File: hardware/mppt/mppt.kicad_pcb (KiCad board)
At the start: 4 copper layers, 90 x 50 mm, 116 parts, among them J1401 Conn_01x04, J1402 Conn_01x02, J1403 Conn_02x04_Odd_Even, J1404 Conn_01x11, J1405 USB_C_Plug_USB2.0, J401 Conn_01x04, J402 Conn_01x03, SW201 SW_SPST, U1401 ISO1044BD, U1402 USBLC6-2SC6, U201 STM32F446RETx, U401 MCP9700Ax-ELT, U402 MCP9700Ax-ELT, Y201 16MHz, Y202 32kHz

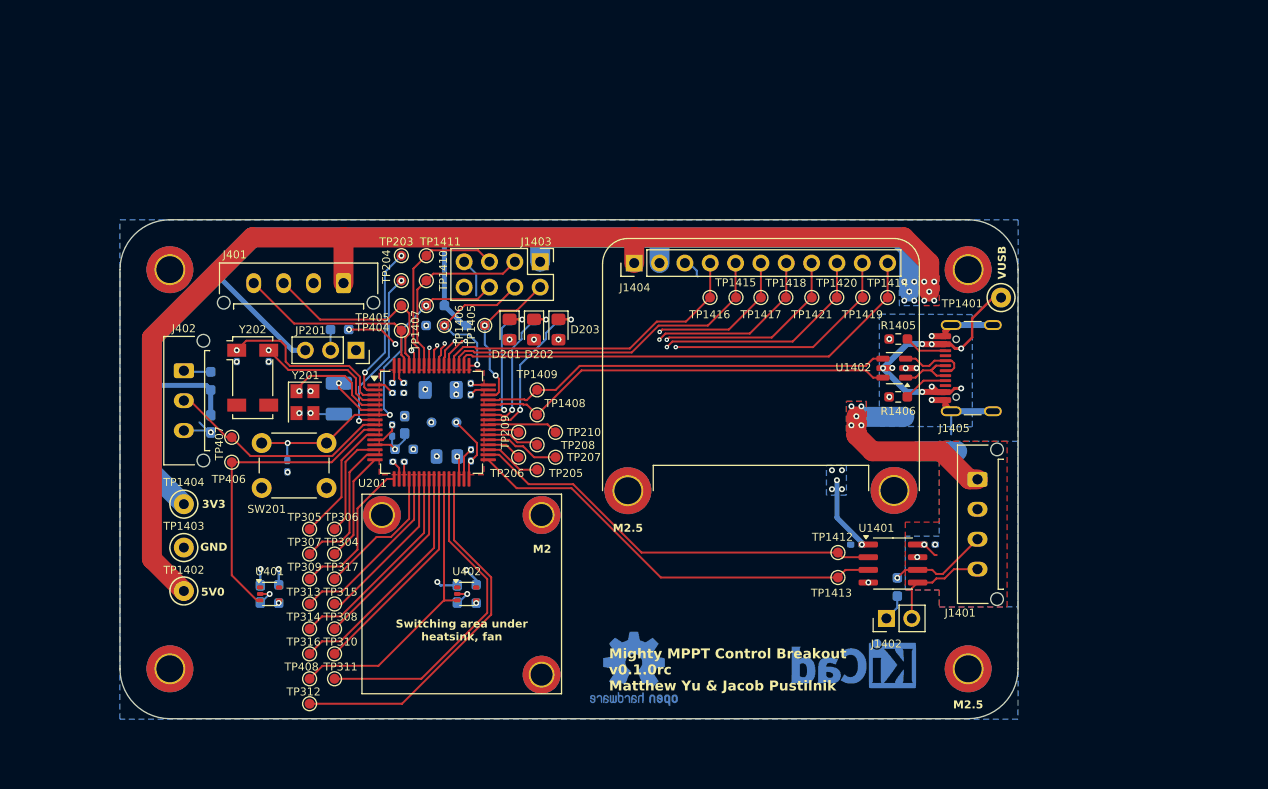
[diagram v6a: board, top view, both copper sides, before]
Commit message: converter schematic and layout.
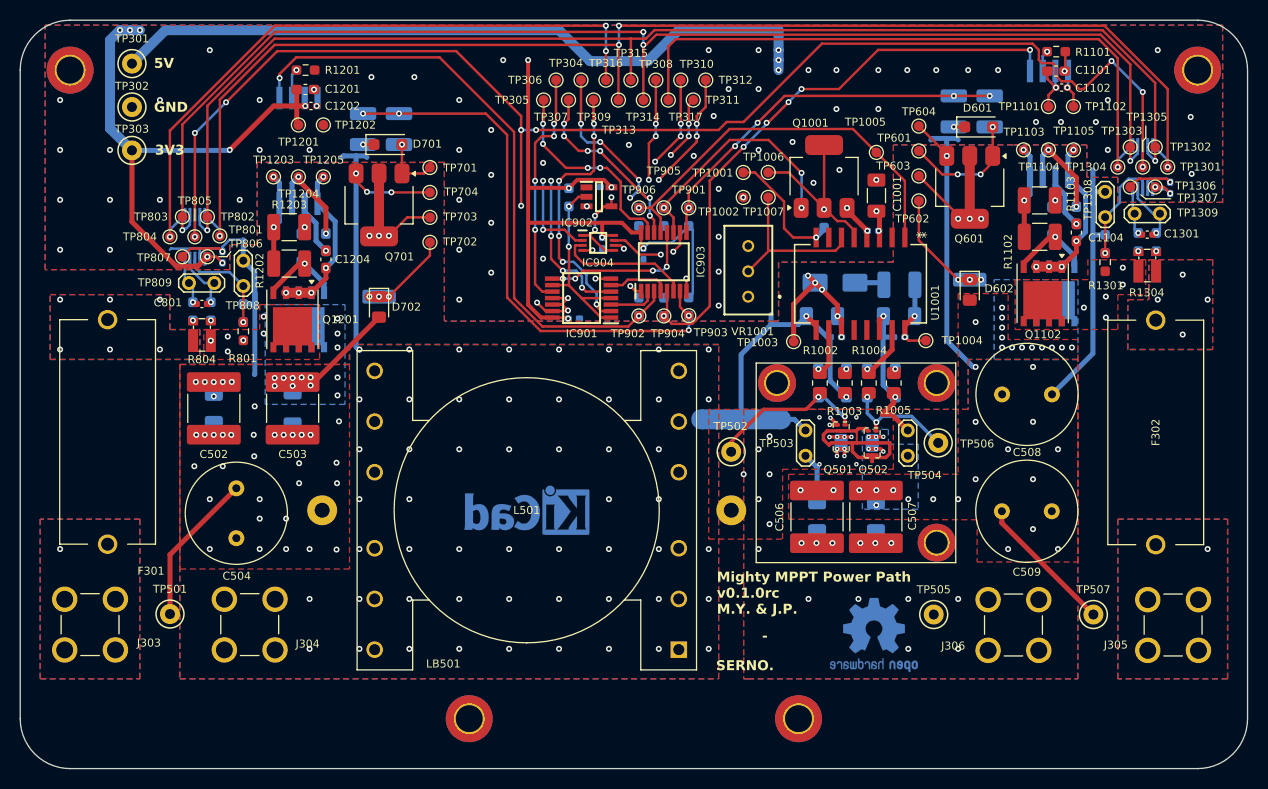
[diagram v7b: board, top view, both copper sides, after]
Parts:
- removed C1401, C1402, C203, C205, C208, C209, C211, C212, C213: 100n, Capacitor_SMD:C_0402_1005Metric_Pad0.74x0.62mm_HandSolder
- removed C201, C206: 10p, Capacitor_SMD:C_0402_1005Metric_Pad0.74x0.62mm_HandSolder
- removed C202, C207: 15p, Capacitor_SMD:C_0402_1005Metric_Pad0.74x0.62mm_HandSolder
- removed C204: 10u, Capacitor_SMD:C_1206_3216Metric_Pad1.33x1.80mm_HandSolder
- removed C210: 4.7u, Capacitor_SMD:C_0805_2012Metric_Pad1.18x1.45mm_HandSolder
- removed C214, C401, C402, C403: 1u, Capacitor_SMD:C_0603_1608Metric_Pad1.08x0.95mm_HandSolder
- removed D201, D202, D203: RED, LED_SMD:LED_0805_2012Metric_Pad1.15x1.40mm_HandSolder
- removed FB201: FerriteBead, Resistor_SMD:R_0603_1608Metric_Pad0.98x0.95mm_HandSolder
- removed H1401, H1402: MountingHole, MountingHole:MountingHole_2.7mm_M2.5_DIN965_Pad_TopBottom
- removed J1401, J401: Conn_01x04, Connector_Molex:Molex_Micro-Fit_3.0_43650-0415_1x04_P3.00mm_Vertical
- removed J1402: Conn_01x02, Connector_PinHeader_2.54mm:PinHeader_1x02_P2.54mm_Vertical
- removed J1403: Conn_02x04_Odd_Even, Connector_PinHeader_2.54mm:PinHeader_2x04_P2.54mm_Vertical
- removed J1404: Conn_01x11, Connector_PinHeader_2.54mm:PinHeader_1x11_P2.54mm_Vertical
- removed J1405: USB_C_Plug_USB2.0, Connector_USB:USB_C_Receptacle_GCT_USB4105-xx-A_16P_TopMnt_Horizontal
- removed J402: Conn_01x03, Connector_Molex:Molex_Micro-Fit_3.0_43650-0315_1x03_P3.00mm_Vertical
- removed JP201: Jumper_3_Bridged12, Connector_PinSocket_2.54mm:PinSocket_1x03_P2.54mm_Vertical
- removed NT1401, NT1402: NetTie_2, NetTie:NetTie-2_SMD_Pad2.0mm
- removed R1401: 120, Resistor_SMD:R_0603_1608Metric_Pad0.98x0.95mm_HandSolder
- removed R1402, R1403, R1404, R204: 100k, Resistor_SMD:R_0603_1608Metric_Pad0.98x0.95mm_HandSolder
- removed R1405, R1406: 5.1k, Resistor_SMD:R_0603_1608Metric_Pad0.98x0.95mm_HandSolder
- removed R201, R202, R205: 3.3k, Resistor_SMD:R_0603_1608Metric_Pad0.98x0.95mm_HandSolder
- removed R203: 0, Resistor_SMD:R_1210_3225Metric_Pad1.30x2.65mm_HandSolder
- removed R401, R402, R403: 205, Resistor_SMD:R_0603_1608Metric_Pad0.98x0.95mm_HandSolder
- removed SW201: SW_SPST, Button_Switch_THT:SW_PUSH_6mm
- removed TP1401, TP1402, TP1403, TP1404: TestPoint, TestPoint:TestPoint_Keystone_5000-5004_Miniature
- removed TP1405, TP1406, TP1407, TP1408, TP1409, TP1410, TP1411, TP1412, TP1413, TP1414, TP1415, TP1416, TP1417, TP1418, TP1419, TP1420, TP1421, TP201, TP202, TP203, TP204, TP205, TP206, TP207, TP208, TP209, TP210, TP404, TP405, TP406, TP407, TP408: TestPoint_Small, TestPoint:TestPoint_Pad_D1.0mm
- removed U1401: ISO1044BD, Package_SO:SOIC-8_3.9x4.9mm_P1.27mm
- removed U1402: USBLC6-2SC6, Package_TO_SOT_SMD:SOT-23-6
- removed U201: STM32F446RETx, Package_QFP:LQFP-64_10x10mm_P0.5mm
- removed U401, U402: MCP9700Ax-ELT, Package_TO_SOT_SMD:SOT-353_SC-70-5
- removed Y201: 16MHz, Crystal:Crystal_SMD_Abracon_ABM8G-4Pin_3.2x2.5mm
- removed Y202: 32kHz, Crystal:Crystal_SMD_Abracon_ABS25-4Pin_8.0x3.8mm
- added C1001: 10u, Capacitor_SMD:C_1206_3216Metric_Pad1.33x1.80mm_HandSolder, F.Cu at (120.8, 42.6)
- added C1002: 100n, Capacitor_SMD:C_0402_1005Metric_Pad0.74x0.62mm_HandSolder, B.Cu at (120.5, 46.1)
- added C1003: 10u, Capacitor_SMD:C_1206_3216Metric_Pad1.33x1.80mm_HandSolder, B.Cu at (123.1, 54.7)
- added C1004: 10u, Capacitor_SMD:C_1206_3216Metric_Pad1.33x1.80mm_HandSolder, B.Cu at (115.3, 54.7)
- added C1005: 100n, Capacitor_SMD:C_0402_1005Metric_Pad0.74x0.62mm_HandSolder, B.Cu at (123.1, 56.8)
- added C1006: 100n, Capacitor_SMD:C_0402_1005Metric_Pad0.74x0.62mm_HandSolder, B.Cu at (116.7, 56.8)
- added C1101: 1u, Capacitor_SMD:C_0603_1608Metric_Pad1.08x0.95mm_HandSolder, F.Cu at (138.8, 30.1)
- added C1102: 100n, Capacitor_SMD:C_0402_1005Metric_Pad0.74x0.62mm_HandSolder, F.Cu at (139.4, 31.8)
- added C1103: 1u, Capacitor_SMD:C_0603_1608Metric_Pad1.08x0.95mm_HandSolder, B.Cu at (140.8, 44.5)
- added C1104: 1u, Capacitor_SMD:C_0603_1608Metric_Pad1.08x0.95mm_HandSolder, F.Cu at (140.8, 46.3)
- added C1201: 1u, Capacitor_SMD:C_0603_1608Metric_Pad1.08x0.95mm_HandSolder, F.Cu at (63.6, 31.9)
- added C1202: 100n, Capacitor_SMD:C_0402_1005Metric_Pad0.74x0.62mm_HandSolder, F.Cu at (64.1, 33.6)
- added C1203: 1u, Capacitor_SMD:C_0603_1608Metric_Pad1.08x0.95mm_HandSolder, B.Cu at (65.6, 47.2)
- added C1204: 1u, Capacitor_SMD:C_0603_1608Metric_Pad1.08x0.95mm_HandSolder, F.Cu at (65.6, 49.0)
- added C1301: 100n, Capacitor_SMD:C_0402_1005Metric_Pad0.74x0.62mm_HandSolder, F.Cu at (147.9, 46.5)
- added C1302: 100n, Capacitor_SMD:C_0402_1005Metric_Pad0.74x0.62mm_HandSolder, B.Cu at (150.2, 41.8)
- added C501: 100n, Capacitor_SMD:C_1206_3216Metric_Pad1.33x1.80mm_HandSolder, B.Cu at (62.3, 63.9)
- added C502: 1u, Capacitor_SMD:C_2220_5750Metric_Pad1.97x5.40mm_HandSolder, F.Cu at (54.4, 63.9)
- added C503: 2.2u, Capacitor_SMD:C_2220_5750Metric_Pad1.97x5.40mm_HandSolder, F.Cu at (62.3, 63.9)
- added C504: 18u, Capacitor_THT:C_Radial_D10.0mm_H16.0mm_P5.00mm, F.Cu at (56.7, 71.9)
- added C505: 100n, Capacitor_SMD:C_1206_3216Metric_Pad1.33x1.80mm_HandSolder, B.Cu at (118.8, 67.4)
- added C506: 1u, Capacitor_SMD:C_2220_5750Metric_Pad1.97x5.40mm_HandSolder, F.Cu at (114.9, 74.8)
- added C507: 2.2u, Capacitor_SMD:C_2220_5750Metric_Pad1.97x5.40mm_HandSolder, F.Cu at (120.8, 74.8)
- added C508: 18u, Capacitor_THT:C_Radial_D10.0mm_H16.0mm_P5.00mm, F.Cu at (133.4, 62.5)
- added C509: 18u, Capacitor_THT:C_Radial_D10.0mm_H16.0mm_P5.00mm, F.Cu at (133.4, 74.2)
- added C801: 100n, Capacitor_SMD:C_0402_1005Metric_Pad0.74x0.62mm_HandSolder, F.Cu at (53.2, 53.4)
- added C802: 100n, Capacitor_SMD:C_0402_1005Metric_Pad0.74x0.62mm_HandSolder, B.Cu at (55.3, 48.8)
- added C901: 100n, Capacitor_SMD:C_0402_1005Metric_Pad0.74x0.62mm_HandSolder, B.Cu at (90.5, 54.9)
- added C902: 100n, Capacitor_SMD:C_0402_1005Metric_Pad0.74x0.62mm_HandSolder, B.Cu at (93.7, 41.7)
- added C903: 100n, Capacitor_SMD:C_0402_1005Metric_Pad0.74x0.62mm_HandSolder, B.Cu at (97.5, 48.4)
- added C904: 100n, Capacitor_SMD:C_0402_1005Metric_Pad0.74x0.62mm_HandSolder, B.Cu at (93.3, 47.3)
- added D1001: Schottky, Diode_SMD:D_SOD-123F, B.Cu at (116.4, 60.0)
- added D1002: Zener, Diode_SMD:D_SOD-123F, B.Cu at (116.4, 62.8)
- added D1003: Schottky, Diode_SMD:D_SOD-123F, B.Cu at (121.3, 60.0)
- added D1004: 0.62V, Diode_SMD:D_SMA, B.Cu at (116.7, 51.3)
- added D1005: Zener, Diode_SMD:D_SOD-123F, B.Cu at (121.3, 62.8)
- added D1101: Schottky, Diode_SMD:D_SOD-123F, B.Cu at (138.5, 45.1)
- added D1201: Schottky, Diode_SMD:D_SOD-123F, B.Cu at (63.2, 47.8)
- added D501: 150, Diode_SMD:D_SMA, B.Cu at (54.4, 63.9)
- added D502: SMAJ150CA, Diode_SMD:D_SMA, B.Cu at (114.9, 74.8)
- added D503: 150, Diode_SMD:D_SMA, B.Cu at (120.8, 74.8)
- added D601: Schottky, Diode_SMD:D_SOD-123F, F.Cu at (131.1, 35.7)
- added D602: BLU, LED_SMD:LED_0805_2012Metric_Pad1.15x1.40mm_HandSolder, F.Cu at (130.2, 52.0)
- added D701: Schottky, Diode_SMD:D_SOD-123F, F.Cu at (71.9, 37.5)
- added D702: BLU, LED_SMD:LED_0805_2012Metric_Pad1.15x1.40mm_HandSolder, F.Cu at (71.0, 53.7)
- added F301: Fuse, footprints:littelfuse_65600001009, F.Cu at (43.8, 66.3)
- added F302: Fuse, footprints:littelfuse_65600001009, F.Cu at (148.8, 66.3)
- added IC1301: INA229AIDGSR, footprints:ti_INA229_AIDGSR, B.Cu at (147.5, 39.7)
- added IC801: INA229AIDGSR, footprints:ti_INA229_AIDGSR, B.Cu at (52.5, 46.7)
- added IC901: SN74LVC08APWR, footprints:ti_SN74LVC08A_PWR, F.Cu at (91.3, 52.9)
- added IC902: SN74LVC1G04DBVR, footprints:ti_SN74LVC1G04_DBVR, F.Cu at (93.0, 42.7)
- added IC903: SN74HCS367PWR, footprints:ti_SN74HCS367_PWR, F.Cu at (99.5, 49.2)
- added IC904: SN74LVC2G32DCUR, footprints:ti_SN74LVC2G32_DCUR, F.Cu at (92.9, 47.3)
- added J303: CT3151, footprints:caltest_ct3151, F.Cu at (42.0, 85.6)
- added J304: CT3151, footprints:caltest_ct3151, F.Cu at (58.0, 85.6)
- added J305: CT3151, footprints:caltest_ct3151, F.Cu at (150.5, 85.6)
- added J306: CT3151, footprints:caltest_ct3151, F.Cu at (134.5, 85.6)
- added L501: 471u, footprints:ferroxcube_PQ32_20_3C97_wire, F.Cu at (62.8, 74.1)
- added LB501: CPV-PQ32/20-1S-12PD-Z, footprints:ferroxcube_CPV-PQ32_20-1S-12P-Z, F.Cu at (101.0, 88.1)
- added NT1001: NetTie_2, NetTie:NetTie-2_SMD_Pad0.5mm, B.Cu at (110.2, 55.0)
- added NT1301: NetTie_2, NetTie:NetTie-2_SMD_Pad0.5mm, B.Cu at (142.5, 40.5)
- added NT501: NetTie_3_Tee, NetTie:NetTie-3_SMD_Pad2.0mm, B.Cu at (107.2, 65.0)
- added NT601: NetTie_2, NetTie:NetTie-2_SMD_Pad0.5mm, B.Cu at (127.8, 37.4)
- added NT701: NetTie_2, NetTie:NetTie-2_SMD_Pad0.5mm, B.Cu at (68.7, 39.1)
- added NT801: NetTie_2, NetTie:NetTie-2_SMD_Pad0.5mm, B.Cu at (57.4, 47.5)
- added Q1001: Q_NMOS_GDS, Package_TO_SOT_SMD:SOT-223-3_TabPin2, F.Cu at (115.6, 40.7)
- added Q1101: Q_NMOS_SGD, Package_SO:PowerPAK_SO-8_Single, B.Cu at (138.7, 52.4)
- added Q1102: Q_NMOS_SGD, Package_SO:PowerPAK_SO-8_Single, F.Cu at (137.5, 52.4)
- added Q1201: Q_NMOS_SGD, Package_SO:PowerPAK_SO-8_Single, F.Cu at (62.3, 55.0)
- added Q1202: Q_NMOS_SGD, Package_SO:PowerPAK_SO-8_Single, B.Cu at (63.5, 55.0)
- added Q501: EPC2059, footprints:epc_EPC2059, F.Cu at (117.3, 66.8)
- added Q502: EPC2059, footprints:epc_EPC2059, F.Cu at (120.4, 67.4)
- added Q601: Q_NMOS_GDS, Package_TO_SOT_SMD:SOT-223-3_TabPin2, F.Cu at (130.2, 41.7)
- added Q701: Q_NMOS_GDS, Package_TO_SOT_SMD:SOT-223-3_TabPin2, F.Cu at (71.0, 43.5)
- added R1001: 100k, Resistor_SMD:R_0603_1608Metric_Pad0.98x0.95mm_HandSolder, B.Cu at (115.6, 44.9)
- added R1002: 0, Resistor_SMD:R_0805_2012Metric_Pad1.20x1.40mm_HandSolder, F.Cu at (115.1, 61.4)
- added R1003: 0, Resistor_SMD:R_0805_2012Metric_Pad1.20x1.40mm_HandSolder, F.Cu at (117.6, 61.4)
- added R1004: 0, Resistor_SMD:R_0805_2012Metric_Pad1.20x1.40mm_HandSolder, F.Cu at (120.0, 61.4)
- added R1005: 0, Resistor_SMD:R_0805_2012Metric_Pad1.20x1.40mm_HandSolder, F.Cu at (122.5, 61.4)
- added R1006: 1.5, Resistor_SMD:R_1210_3225Metric_Pad1.30x2.65mm_HandSolder, B.Cu at (123.1, 51.5)
- added R1101: 7.32k, Resistor_SMD:R_0603_1608Metric_Pad0.98x0.95mm_HandSolder, F.Cu at (138.8, 28.1)
- added R1102: 15, Resistor_SMD:R_1210_3225Metric_Pad1.30x2.65mm_HandSolder, F.Cu at (137.2, 46.7)
- added R1103: 15, Resistor_SMD:R_1210_3225Metric_Pad1.30x2.65mm_HandSolder, F.Cu at (137.2, 43.1)
- added R1201: 7.32k, Resistor_SMD:R_0603_1608Metric_Pad0.98x0.95mm_HandSolder, F.Cu at (63.6, 30.0)
- added R1202: 15, Resistor_SMD:R_1210_3225Metric_Pad1.30x2.65mm_HandSolder, F.Cu at (62.0, 49.4)
- added R1203: 15, Resistor_SMD:R_1210_3225Metric_Pad1.30x2.65mm_HandSolder, F.Cu at (62.0, 45.7)
- added R1301: 86.6k, Resistor_SMD:R_0603_1608Metric_Pad0.98x0.95mm_HandSolder, F.Cu at (143.7, 49.3)
- added R1302: 100k, Resistor_SMD:R_0603_1608Metric_Pad0.98x0.95mm_HandSolder, B.Cu at (143.7, 47.4)
- added R1303: 15, Resistor_SMD:R_0603_1608Metric_Pad0.98x0.95mm_HandSolder, B.Cu at (147.1, 47.2)
- added R1304: 4m, Resistor_SMD:R_Shunt_Vishay_WSKW0612, F.Cu at (147.9, 49.6)
- added R1305: 15, Resistor_SMD:R_0603_1608Metric_Pad0.98x0.95mm_HandSolder, B.Cu at (148.8, 47.2)
- added R601: 15, Resistor_SMD:R_1210_3225Metric_Pad1.30x2.65mm_HandSolder, B.Cu at (128.6, 34.1)
- added R602: 15, Resistor_SMD:R_1210_3225Metric_Pad1.30x2.65mm_HandSolder, B.Cu at (132.2, 34.1)
- added R603: 10k, Resistor_SMD:R_2512_6332Metric_Pad1.40x3.35mm_HandSolder, B.Cu at (130.2, 48.0)
- added R701: 15, Resistor_SMD:R_1210_3225Metric_Pad1.30x2.65mm_HandSolder, B.Cu at (69.4, 35.9)
- added R702: 15, Resistor_SMD:R_1210_3225Metric_Pad1.30x2.65mm_HandSolder, B.Cu at (73.0, 35.9)
- added R703: 10k, Resistor_SMD:R_2512_6332Metric_Pad1.40x3.35mm_HandSolder, B.Cu at (71.0, 49.7)
- added R801: 86.6k, Resistor_SMD:R_0603_1608Metric_Pad0.98x0.95mm_HandSolder, F.Cu at (57.4, 56.2)
- added R802: 100k, Resistor_SMD:R_0603_1608Metric_Pad0.98x0.95mm_HandSolder, B.Cu at (57.4, 54.4)
- added R803: 15, Resistor_SMD:R_0603_1608Metric_Pad0.98x0.95mm_HandSolder, B.Cu at (52.3, 54.2)
- added R804: 4m, Resistor_SMD:R_Shunt_Vishay_WSKW0612, F.Cu at (53.2, 56.5)
- added R805: 15, Resistor_SMD:R_0603_1608Metric_Pad0.98x0.95mm_HandSolder, B.Cu at (54.1, 54.2)
- added R901: 100k, Resistor_SMD:R_0603_1608Metric_Pad0.98x0.95mm_HandSolder, B.Cu at (90.0, 42.8)
- added R902: 100k, Resistor_SMD:R_0603_1608Metric_Pad0.98x0.95mm_HandSolder, B.Cu at (102.0, 44.7)
- added R903: 100k, Resistor_SMD:R_0603_1608Metric_Pad0.98x0.95mm_HandSolder, B.Cu at (97.0, 53.7)
- added R904: 100k, Resistor_SMD:R_0603_1608Metric_Pad0.98x0.95mm_HandSolder, B.Cu at (102.0, 53.7)
- added R905: 100k, Resistor_SMD:R_0603_1608Metric_Pad0.98x0.95mm_HandSolder, B.Cu at (99.5, 53.7)
- added R906: 100k, Resistor_SMD:R_0603_1608Metric_Pad0.98x0.95mm_HandSolder, B.Cu at (99.5, 44.7)
- added R907: 100k, Resistor_SMD:R_0603_1608Metric_Pad0.98x0.95mm_HandSolder, B.Cu at (97.0, 44.7)
- added TP1001: TestPoint_Small, TestPoint:TestPoint_Pad_D1.0mm, F.Cu at (107.5, 40.3)
- added TP1002: TestPoint_Small, TestPoint:TestPoint_Pad_D1.0mm, F.Cu at (107.5, 42.8)
- added TP1003: TestPoint_Small, TestPoint:TestPoint_Pad_D1.0mm, F.Cu at (112.5, 57.2)
- added TP1004: TestPoint_Small, TestPoint:TestPoint_Pad_D1.0mm, F.Cu at (125.8, 57.1)
- added TP1005: TestPoint_Small, TestPoint:TestPoint_Pad_D1.0mm, F.Cu at (120.8, 38.2)
- added TP1006: TestPoint_Small, TestPoint:TestPoint_Pad_D1.0mm, F.Cu at (110.0, 40.3)
- added TP1007: TestPoint_Small, TestPoint:TestPoint_Pad_D1.0mm, F.Cu at (110.0, 42.8)
- added TP1101: TestPoint_Small, TestPoint:TestPoint_Pad_D1.0mm, F.Cu at (138.1, 33.6)
- added TP1102: TestPoint_Small, TestPoint:TestPoint_Pad_D1.0mm, F.Cu at (140.6, 33.6)
- added TP1103: TestPoint_Small, TestPoint:TestPoint_Pad_D1.0mm, F.Cu at (135.6, 38.0)
- added TP1104: TestPoint_Small, TestPoint:TestPoint_Pad_D1.0mm, F.Cu at (138.1, 38.0)
- added TP1105: TestPoint_Small, TestPoint:TestPoint_Pad_D1.0mm, F.Cu at (140.6, 38.0)
- added TP1201: TestPoint_Small, TestPoint:TestPoint_Pad_D1.0mm, F.Cu at (62.9, 35.5)
- added TP1202: TestPoint_Small, TestPoint:TestPoint_Pad_D1.0mm, F.Cu at (65.4, 35.5)
- added TP1203: TestPoint_Small, TestPoint:TestPoint_Pad_D1.0mm, F.Cu at (60.4, 40.7)
- added TP1204: TestPoint_Small, TestPoint:TestPoint_Pad_D1.0mm, F.Cu at (62.9, 40.7)
- added TP1205: TestPoint_Small, TestPoint:TestPoint_Pad_D1.0mm, F.Cu at (65.4, 40.7)
- added TP1301: TestPoint_Small, TestPoint:TestPoint_Pad_D1.0mm, F.Cu at (150.0, 39.7)
- added TP1302: TestPoint_Small, TestPoint:TestPoint_Pad_D1.0mm, F.Cu at (148.7, 37.7)
- added TP1303: TestPoint_Small, TestPoint:TestPoint_Pad_D1.0mm, F.Cu at (146.2, 37.7)
- added TP1304: TestPoint_Small, TestPoint:TestPoint_Pad_D1.0mm, F.Cu at (145.0, 39.7)
- added TP1305: TestPoint_Small, TestPoint:TestPoint_Pad_D1.0mm, F.Cu at (147.5, 39.7)
- added TP1306: TestPoint_Small, TestPoint:TestPoint_Pad_D1.0mm, F.Cu at (148.7, 41.7)
- added TP1307: TestPoint_Small, TestPoint:TestPoint_Pad_D1.0mm, F.Cu at (146.2, 41.7)
- added TP1308: TestPoint_2Pole, TestPoint:TestPoint_2Pads_Pitch2.54mm_Drill0.8mm, F.Cu at (143.7, 44.7)
- added TP1309: TestPoint_2Pole, TestPoint:TestPoint_2Pads_Pitch2.54mm_Drill0.8mm, F.Cu at (146.7, 44.4)
- added TP301: TestPoint, TestPoint:TestPoint_Keystone_5000-5004_Miniature, F.Cu at (46.2, 29.4)
- added TP302: TestPoint, TestPoint:TestPoint_Keystone_5000-5004_Miniature, F.Cu at (46.2, 33.7)
- added TP303: TestPoint, TestPoint:TestPoint_Keystone_5000-5004_Miniature, F.Cu at (46.2, 38.0)
- added TP501: TestPoint, TestPoint:TestPoint_Keystone_5000-5004_Miniature, F.Cu at (50.0, 84.5)
- added TP502: TestPoint, TestPoint:TestPoint_Keystone_5000-5004_Miniature, F.Cu at (106.2, 68.2)
- added TP503: TestPoint_2Pole, TestPoint:TestPoint_2Pads_Pitch2.54mm_Drill0.8mm, F.Cu at (113.7, 66.1)
- added TP504: TestPoint_2Pole, TestPoint:TestPoint_2Pads_Pitch2.54mm_Drill0.8mm, F.Cu at (124.0, 66.1)
- added TP505: TestPoint, TestPoint:TestPoint_Keystone_5000-5004_Miniature, F.Cu at (126.5, 84.6)
- added TP506: TestPoint, TestPoint:TestPoint_Keystone_5000-5004_Miniature, F.Cu at (127.0, 67.4)
- added TP507: TestPoint, TestPoint:TestPoint_Keystone_5000-5004_Miniature, F.Cu at (142.6, 84.6)
- added TP601: TestPoint_Small, TestPoint:TestPoint_Pad_D1.0mm, F.Cu at (125.1, 38.1)
- added TP602: TestPoint_Small, TestPoint:TestPoint_Pad_D1.0mm, F.Cu at (125.1, 43.1)
- added TP603: TestPoint_Small, TestPoint:TestPoint_Pad_D1.0mm, F.Cu at (125.1, 40.6)
- added TP604: TestPoint_Small, TestPoint:TestPoint_Pad_D1.0mm, F.Cu at (125.1, 35.6)
- added TP701: TestPoint_Small, TestPoint:TestPoint_Pad_D1.0mm, F.Cu at (76.1, 39.8)
- added TP702: TestPoint_Small, TestPoint:TestPoint_Pad_D1.0mm, F.Cu at (76.1, 47.3)
- added TP703: TestPoint_Small, TestPoint:TestPoint_Pad_D1.0mm, F.Cu at (76.1, 44.8)
- added TP704: TestPoint_Small, TestPoint:TestPoint_Pad_D1.0mm, F.Cu at (76.1, 42.3)
- added TP801: TestPoint_Small, TestPoint:TestPoint_Pad_D1.0mm, F.Cu at (55.0, 46.6)
- added TP802: TestPoint_Small, TestPoint:TestPoint_Pad_D1.0mm, F.Cu at (53.8, 44.7)
- added TP803: TestPoint_Small, TestPoint:TestPoint_Pad_D1.0mm, F.Cu at (51.3, 44.7)
- added TP804: TestPoint_Small, TestPoint:TestPoint_Pad_D1.0mm, F.Cu at (50.0, 46.7)
- added TP805: TestPoint_Small, TestPoint:TestPoint_Pad_D1.0mm, F.Cu at (52.5, 46.7)
- added TP806: TestPoint_Small, TestPoint:TestPoint_Pad_D1.0mm, F.Cu at (53.8, 48.7)
- added TP807: TestPoint_Small, TestPoint:TestPoint_Pad_D1.0mm, F.Cu at (51.3, 48.7)
- added TP808: TestPoint_2Pole, TestPoint:TestPoint_2Pads_Pitch2.54mm_Drill0.8mm, F.Cu at (57.4, 51.6)
- added TP809: TestPoint_2Pole, TestPoint:TestPoint_2Pads_Pitch2.54mm_Drill0.8mm, F.Cu at (51.9, 51.3)
- added TP901: TestPoint_Small, TestPoint:TestPoint_Pad_D1.0mm, F.Cu at (102.0, 43.8)
- added TP902: TestPoint_Small, TestPoint:TestPoint_Pad_D1.0mm, F.Cu at (97.0, 54.6)
- added TP903: TestPoint_Small, TestPoint:TestPoint_Pad_D1.0mm, F.Cu at (102.0, 54.6)
- added TP904: TestPoint_Small, TestPoint:TestPoint_Pad_D1.0mm, F.Cu at (99.5, 54.6)
- added TP905: TestPoint_Small, TestPoint:TestPoint_Pad_D1.0mm, F.Cu at (99.5, 43.8)
- added TP906: TestPoint_Small, TestPoint:TestPoint_Pad_D1.0mm, F.Cu at (97.0, 43.8)
- added U1001: ADUM4221-1ARIZ, footprints:ad_ADUM4221_1ARIZ, F.Cu at (119.2, 51.4)
- added U1101: TPSI3050, footprints:ti_TPS3050_DWZ, B.Cu at (138.1, 35.4)
- added U1201: TPSI3050, footprints:ti_TPS3050_DWZ, B.Cu at (62.9, 38.1)
- added VR1001: PV36W104C01B00, footprints:bourns_PV36W201C01B00, F.Cu at (108.0, 52.7)
- moved TP312 74.0 mm to (103.7, 31.0)
- moved TP311 68.2 mm to (102.5, 33.0)
- moved TP310 67.2 mm to (101.2, 31.0)
- moved TP316 64.7 mm to (93.7, 31.0), turned to 90 degrees
- moved TP308 63.7 mm to (98.7, 31.0)
- moved TP314 62.7 mm to (97.5, 33.0), turned to 90 degrees
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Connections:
- TP316 pad 1: /MON_OUT_CS -> /MON_IN_CS
- TP317 pad 1: /MON_IN_CS -> /MON_OUT_CS
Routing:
- net /power_converter/~{MON_ALERT}: track 0.00 -> 166.5 mm, vias 0 -> 11
- net /MON_SPI_CLK: track 18.0 -> 134.4 mm, vias 0 -> 4
- net /MON_SPI_CIPO: track 16.4 -> 128.6 mm, vias 0 -> 2
- net /MON_SPI_COPI: track 20.9 -> 131.5 mm, vias 0 -> 4
- net /power_converter/LS_SRC_EN_BUF: track 0.00 -> 63.6 mm, vias 0 -> 2
- net /power_converter/OUT-: track 0.00 -> 63.2 mm, vias 0 -> 33
- net /power_converter/LS_SNK_EN_BUF: track 0.00 -> 60.6 mm, vias 0 -> 6
- net /power_converter/AL_SRC_EN_BUF: track 0.00 -> 55.5 mm, vias 0 -> 4
- net /MON_IN_CS: track 14.0 -> 67.0 mm, vias 0 -> 3
- net /SDC_CS: track 51.9 -> 0.00 mm, vias 2 -> 0
- net /BACKLIGHT_PWM: track 49.3 -> 0.00 mm
- net /DC: track 48.6 -> 0.00 mm, vias 2 -> 0
- net /RESET: track 45.4 -> 0.00 mm, vias 2 -> 0
- net /power_converter/VSW: track 0.00 -> 44.3 mm, vias 0 -> 10
- net +5V: track 155.0 -> 111.2 mm, vias 11 -> 8
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- added copper zone on B.Cu, net /VI+
- added copper zone on F.Cu, net /VI+
- added copper zone on In1.Cu, net /VI+
- added copper zone on In2.Cu, net /VI+
- added copper zone on B.Cu, net /VI-
- added copper zone on F.Cu, net /VI-
- added copper zone on In1.Cu, net /VI-
- added copper zone on In2.Cu, net /VI-
- added copper zone on B.Cu, net /power_converter/Active Load Sink/V+
- added copper zone on F.Cu, net /power_converter/Active Load Sink/V+
- added copper zone on In1.Cu, net /power_converter/Active Load Sink/V+
- added copper zone on In2.Cu, net /power_converter/Active Load Sink/V+
- added copper zone on B.Cu, net /power_converter/Active Load Source/V+
- added copper zone on F.Cu, net /power_converter/Active Load Source/V+
- added copper zone on In1.Cu, net /power_converter/Active Load Source/V+
- added copper zone on In2.Cu, net /power_converter/Active Load Source/V+
- added copper zone on F.Cu, net /power_converter/Load Switch Sink/I+
- added copper zone on In1.Cu, net /power_converter/Load Switch Sink/I+
- added copper zone on F.Cu, net /power_converter/Load Switch Source/I-
- added copper zone on In1.Cu, net /power_converter/Load Switch Source/I-
- added copper zone on B.Cu, net /power_converter/OUT+
- added copper zone on F.Cu, net /power_converter/OUT+
- added copper zone on In1.Cu, net /power_converter/OUT+
- added copper zone on In2.Cu, net /power_converter/OUT+
- added copper zone on B.Cu, net /power_converter/OUT-
- added copper zone on F.Cu, net /power_converter/OUT-
- added copper zone on In1.Cu, net /power_converter/OUT-
- added copper zone on In2.Cu, net /power_converter/OUT-
- added copper zone on B.Cu, net /power_converter/Power Monitor Sink/I-
- added copper zone on F.Cu, net /power_converter/Power Monitor Sink/I-
- added copper zone on In1.Cu, net /power_converter/Power Monitor Sink/I-
- added copper zone on In2.Cu, net /power_converter/Power Monitor Sink/I-
- added copper zone on F.Cu, net /power_converter/VSW
- added copper zone on In1.Cu, net /power_converter/VSW
- added copper zone on B.Cu, net /power_converter/_IN+
- added copper zone on F.Cu, net /power_converter/_IN+
- added copper zone on In1.Cu, net /power_converter/_IN+
- added copper zone on In2.Cu, net /power_converter/_IN+
- added copper zone on F.Cu, net GND
- removed copper zone on B.Cu, net +3V3
- removed copper zone on F.Cu, net +3V3
- removed copper zone on In1.Cu, net +3V3
- removed copper zone on In2.Cu, net +3V3
- removed copper zone on B.Cu, net +5V
- removed copper zone on F.Cu, net +5V
- removed copper zone on In1.Cu, net +5V
- removed copper zone on B.Cu, net /VUSB
- removed copper zone on B.Cu, net GND1
- removed copper zone on In1.Cu, net GND1
- removed copper zone on In2.Cu, net GND1
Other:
- board size 90 x 50 mm -> 123 x 75 mm
- board text added: "*"
- board text added: "-"
- board text added: "5V"
- board text added: "Mighty MPPT Power Path v0.1.0rc M.Y. & J.P."
- board text added: "SERNO."
- board text removed: "5V0"
- board text removed: "M2"
- board text removed: "M2.5"
- board text removed: "Mighty MPPT Control Breakout v0.1.0rc Matthew Yu & Jacob Pustilnik"
- board text removed: "Swap down to 0603."
- board text removed: "Switching area under heatsink, fan"
- board text removed: "VUSB"

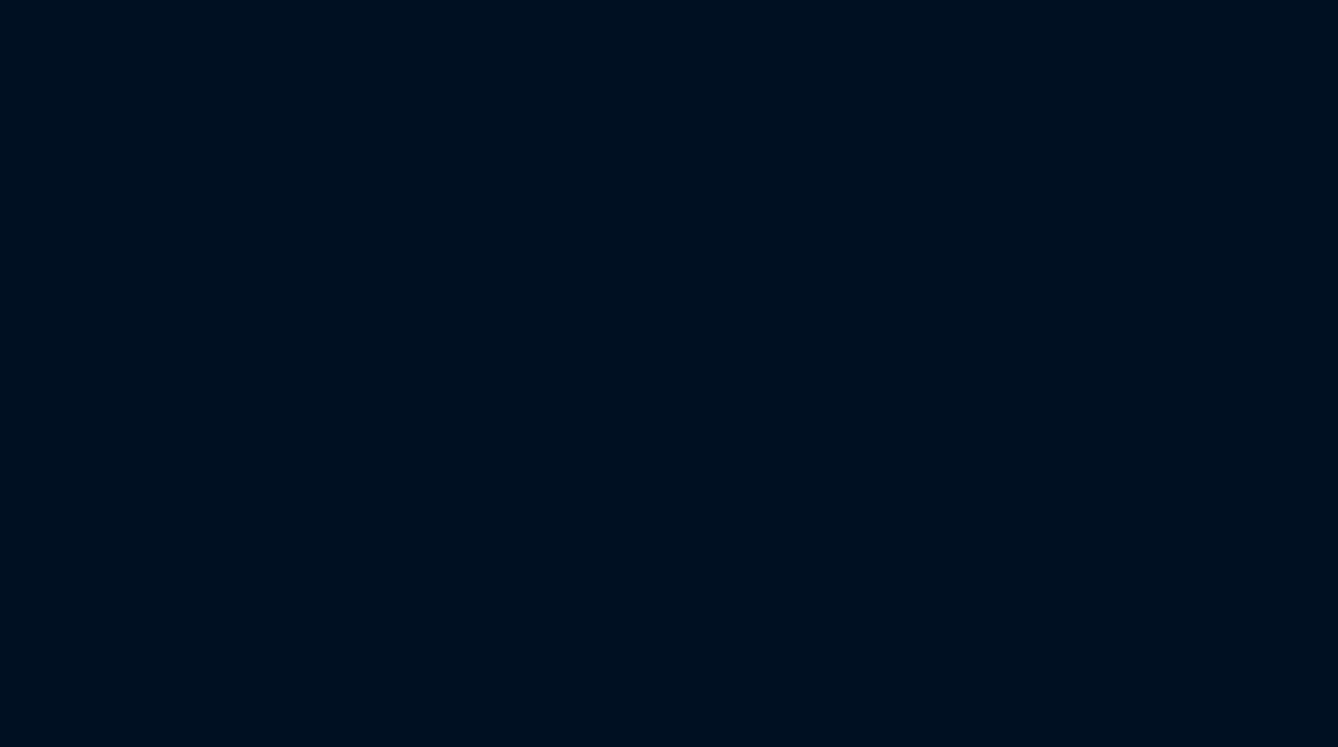
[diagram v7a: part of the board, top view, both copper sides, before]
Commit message: pull in tft, power reg layouts
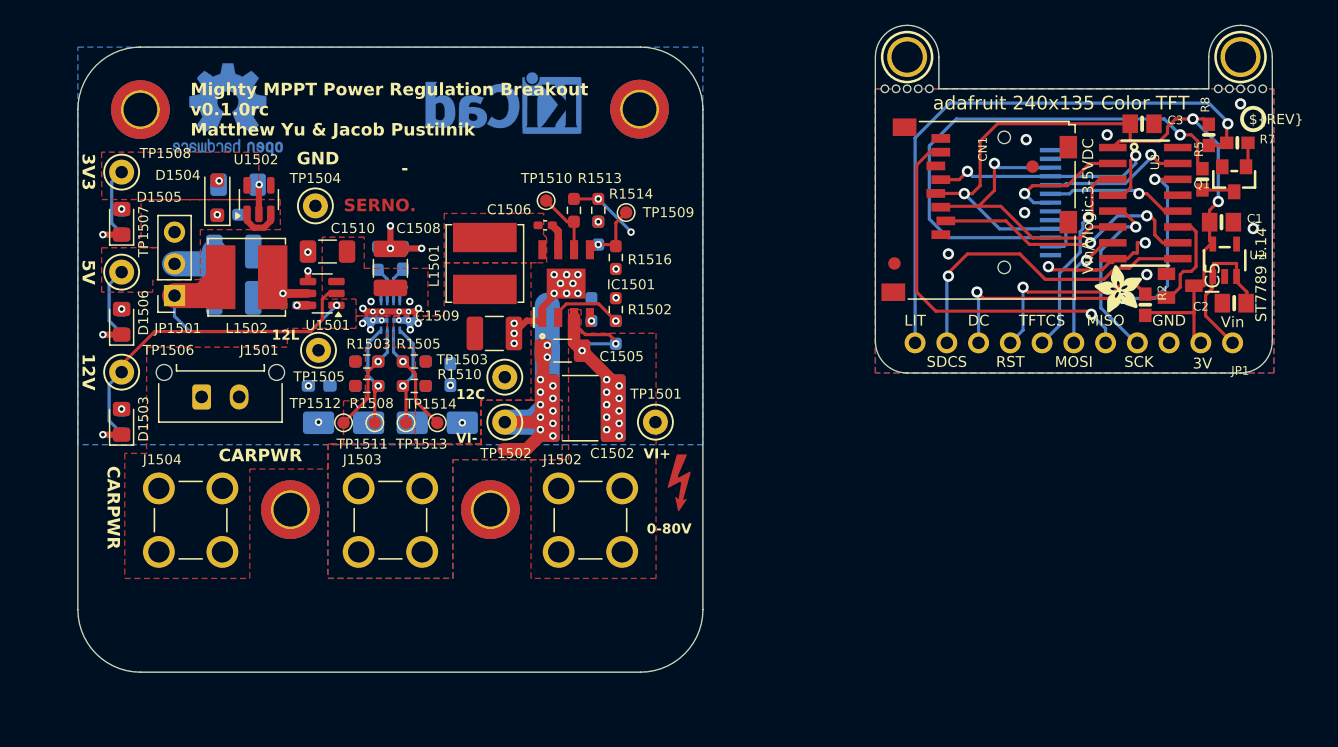
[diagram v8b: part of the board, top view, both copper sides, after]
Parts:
- added @HOLE0: , , F.Cu at (236.0, 25.6)
- added @HOLE1: , , F.Cu at (235.1, 25.6)
- added @HOLE2: , , F.Cu at (234.2, 25.6)
- added @HOLE3: , , F.Cu at (233.3, 25.6)
- added @HOLE4: , , F.Cu at (232.5, 25.6)
- added @HOLE5: , , F.Cu at (262.7, 25.6)
- added @HOLE6: , , F.Cu at (261.8, 25.6)
- added @HOLE7: , , F.Cu at (260.9, 25.6)
- added @HOLE8: , , F.Cu at (260.0, 25.6)
- added @HOLE9: , , F.Cu at (259.1, 25.6)
- added C1: 10µF, Adafruit 1.14-inch 240x135 Color TFT:0805-NO, F.Cu at (259.4, 36.3)
- added C1501: 1u, Capacitor_SMD:C_0603_1608Metric_Pad1.08x0.95mm_HandSolder, B.Cu at (187.2, 49.4)
- added C1502: 2.2u, Capacitor_SMD:C_2220_5750Metric_Pad1.97x5.40mm_HandSolder, F.Cu at (208.1, 51.2)
- added C1503: 2.2u, Capacitor_SMD:C_2220_5750Metric_Pad1.97x5.40mm_HandSolder, B.Cu at (208.1, 51.2)
- added C1504: 1u, Capacitor_SMD:C_0603_1608Metric_Pad1.08x0.95mm_HandSolder, B.Cu at (197.7, 48.5)
- added C1505: 100n, Capacitor_SMD:C_1206_3216Metric_Pad1.33x1.80mm_HandSolder, F.Cu at (206.7, 46.6)
- added C1506: 100n, Capacitor_SMD:C_0402_1005Metric_Pad0.74x0.62mm_HandSolder, F.Cu at (205.3, 36.6)
- added C1507: 1u, Capacitor_SMD:C_0603_1608Metric_Pad1.08x0.95mm_HandSolder, B.Cu at (193.9, 39.2)
- added C1508: 22u, Capacitor_SMD:C_1210_3225Metric_Pad1.33x2.70mm_HandSolder, F.Cu at (192.9, 40.0)
- added C1509: 22u, Capacitor_SMD:C_1210_3225Metric_Pad1.33x2.70mm_HandSolder, F.Cu at (201.2, 45.2)
- added C1510: 10u, Capacitor_SMD:C_1206_3216Metric_Pad1.33x1.80mm_HandSolder, F.Cu at (187.9, 38.7)
- added C1511: 1u, Capacitor_SMD:C_0603_1608Metric_Pad1.08x0.95mm_HandSolder, B.Cu at (179.9, 35.7)
- added C1512: 10u, Capacitor_SMD:C_1206_3216Metric_Pad1.33x1.80mm_HandSolder, B.Cu at (180.7, 33.3)
- added C1513: 100n, Capacitor_SMD:C_0402_1005Metric_Pad0.74x0.62mm_HandSolder, B.Cu at (184.9, 43.0)
- added C1514: 22u, Capacitor_SMD:C_1210_3225Metric_Pad1.33x2.70mm_HandSolder, B.Cu at (180.4, 38.7)
- added C1515: 22u, Capacitor_SMD:C_1210_3225Metric_Pad1.33x2.70mm_HandSolder, B.Cu at (180.4, 42.4)
- added C2: 10µF, Adafruit 1.14-inch 240x135 Color TFT:0805-NO, F.Cu at (260.4, 42.8)
- added C3: 0.1uF, Adafruit 1.14-inch 240x135 Color TFT:0805-NO, F.Cu at (253.0, 28.4)
- added CN1: , Adafruit 1.14-inch 240x135 Color TFT:MICROSD, F.Cu at (247.6, 28.3)
- added D1501: SMAJ15CA, Diode_SMD:D_SMA, B.Cu at (189.2, 52.4)
- added D1502: SMAJ15CA, Diode_SMD:D_SMA, B.Cu at (196.7, 52.4)
- added D1503: RED, LED_SMD:LED_0805_2012Metric_Pad1.15x1.40mm_HandSolder, F.Cu at (171.4, 52.3)
- added D1504: Schottky, Diode_SMD:D_SOD-123F, F.Cu at (179.1, 34.3)
- added D1505: RED, LED_SMD:LED_0805_2012Metric_Pad1.15x1.40mm_HandSolder, F.Cu at (171.4, 36.3)
- added D1506: RED, LED_SMD:LED_0805_2012Metric_Pad1.15x1.40mm_HandSolder, F.Cu at (171.4, 44.3)
- added DISP1: DISP_LCD_GENERIC_SPI_1.14IN_240X135_WRAPUNDER, Adafruit 1.14-inch 240x135 Color TFT:TFT_1.14IN_240X135_WRAPUNDER, B.Cu at (232.2, 34.8)
- added FID1: FIDUCIAL_1MM, Adafruit 1.14-inch 240x135 Color TFT:FIDUCIAL_1MM, F.Cu at (233.2, 39.6)
- added FID2: FIDUCIAL_1MM, Adafruit 1.14-inch 240x135 Color TFT:FIDUCIAL_1MM, F.Cu at (244.3, 31.9)
- added H101: MountingHole, MountingHole:MountingHole_2.7mm_M2.5_DIN965_Pad_TopBottom, F.Cu at (172.9, 27.3)
- added H102: MountingHole, MountingHole:MountingHole_2.7mm_M2.5_DIN965_Pad_TopBottom, F.Cu at (212.8, 27.3)
- added H103: MountingHole, MountingHole:MountingHole_2.7mm_M2.5_DIN965_Pad_TopBottom, F.Cu at (184.9, 59.3)
- added H104: MountingHole, MountingHole:MountingHole_2.7mm_M2.5_DIN965_Pad_TopBottom, F.Cu at (200.9, 59.3)
- added IC1501: LMR38010SDDAR, footprints:ti_LMR38010_SDDAR, F.Cu at (207.0, 41.2)
- added IC1502: TPS2121, footprints:ti_TPS2121_RUXR, B.Cu at (192.9, 43.8)
- added IC5: APX803, Adafruit 1.14-inch 240x135 Color TFT:SOT23, F.Cu at (256.1, 41.4)
- added J1501: Conn_01x02, Connector_Molex:Molex_Micro-Fit_3.0_43650-0215_1x02_P3.00mm_Vertical, F.Cu at (177.8, 50.3)
- added J1502: CT3151, footprints:caltest_ct3151, F.Cu at (208.9, 60.1)
- added J1503: CT3151, footprints:caltest_ct3151, F.Cu at (192.9, 60.1)
- added J1504: CT3151, footprints:caltest_ct3151, F.Cu at (176.9, 60.1)
- added JP1: , Adafruit 1.14-inch 240x135 Color TFT:1X11_ROUND, F.Cu at (247.6, 46.0)
- added JP1501: Jumper_3_Bridged12, Connector_PinSocket_2.54mm:PinSocket_1x03_P2.54mm_Vertical, F.Cu at (175.6, 42.2)
- added L1501: 68u, Inductor_SMD:L_Bourns_SRN6045TA, F.Cu at (200.5, 39.6)
- added L1502: 4.7u, Inductor_SMD:L_Bourns_SRN6045TA, F.Cu at (181.4, 40.7)
- added NT1501: NetTie_2, NetTie:NetTie-2_SMD_Pad2.0mm, B.Cu at (205.4, 45.0)
- added Q1: MMBT2222, Adafruit 1.14-inch 240x135 Color TFT:SOT23-WIDE, F.Cu at (260.4, 32.9)
- added R1501: 100k, Resistor_SMD:R_0603_1608Metric_Pad0.98x0.95mm_HandSolder, B.Cu at (210.9, 45.1)
- added R1502: 10k, Resistor_SMD:R_0603_1608Metric_Pad0.98x0.95mm_HandSolder, F.Cu at (210.9, 43.3)
- added R1503: 100k, Resistor_SMD:R_0603_1608Metric_Pad0.98x0.95mm_HandSolder, F.Cu at (191.0, 47.5)
- added R1504: 7.68k, Resistor_SMD:R_0603_1608Metric_Pad0.98x0.95mm_HandSolder, B.Cu at (191.0, 47.5)
- added R1505: 100k, Resistor_SMD:R_0603_1608Metric_Pad0.98x0.95mm_HandSolder, F.Cu at (194.8, 47.5)
- added R1506: 7.68k, Resistor_SMD:R_0603_1608Metric_Pad0.98x0.95mm_HandSolder, B.Cu at (194.8, 47.5)
- added R1507: 64.9k, Resistor_SMD:R_0603_1608Metric_Pad0.98x0.95mm_HandSolder, B.Cu at (209.0, 43.3)
- added R1508: 100k, Resistor_SMD:R_0603_1608Metric_Pad0.98x0.95mm_HandSolder, F.Cu at (191.0, 49.4)
- added R1509: 17.4k, Resistor_SMD:R_0603_1608Metric_Pad0.98x0.95mm_HandSolder, B.Cu at (191.0, 49.4)
- added R1510: 100k, Resistor_SMD:R_0603_1608Metric_Pad0.98x0.95mm_HandSolder, F.Cu at (194.8, 49.4)
- added R1511: 14k, Resistor_SMD:R_0603_1608Metric_Pad0.98x0.95mm_HandSolder, B.Cu at (194.8, 49.4)
- added R1512: 64.9k, Resistor_SMD:R_0603_1608Metric_Pad0.98x0.95mm_HandSolder, B.Cu at (191.9, 39.2)
- added R1513: 100k, Resistor_SMD:R_0603_1608Metric_Pad0.98x0.95mm_HandSolder, F.Cu at (207.6, 35.4)
- added R1514: 100k, Resistor_SMD:R_0603_1608Metric_Pad0.98x0.95mm_HandSolder, F.Cu at (209.5, 35.4)
- added R1515: 10k, Resistor_SMD:R_0603_1608Metric_Pad0.98x0.95mm_HandSolder, B.Cu at (209.5, 37.2)
- added R1516: 10k, Resistor_SMD:R_0603_1608Metric_Pad0.98x0.95mm_HandSolder, F.Cu at (210.9, 39.1)
- added R1517: 10k, Resistor_SMD:R_0603_1608Metric_Pad0.98x0.95mm_HandSolder, B.Cu at (171.4, 52.3)
- added R1518: 3.3k, Resistor_SMD:R_0603_1608Metric_Pad0.98x0.95mm_HandSolder, B.Cu at (171.4, 36.3)
- added R1519: 3.3k, Resistor_SMD:R_0603_1608Metric_Pad0.98x0.95mm_HandSolder, B.Cu at (171.4, 44.3)
- added R2: 10K, Adafruit 1.14-inch 240x135 Color TFT:0603-NO, F.Cu at (253.3, 42.9)
- added R5: 22, Adafruit 1.14-inch 240x135 Color TFT:0603-NO, F.Cu at (257.9, 32.9)
- added R7: 1K, Adafruit 1.14-inch 240x135 Color TFT:0603-NO, F.Cu at (260.6, 30.0)
- added R8: 10K, Adafruit 1.14-inch 240x135 Color TFT:0603-NO, F.Cu at (258.4, 29.3)
- added REF**: Symbol_HighVoltage_NoTriangle_2x5mm_Copper, Symbol:Symbol_HighVoltage_NoTriangle_2x5mm_Copper, F.Cu at (216.2, 57.3)
- added REF**: OSHW-Logo2_9.8x8mm_Copper, Symbol:OSHW-Logo2_9.8x8mm_Copper, B.Cu at (179.9, 27.3)
- added REF**: KiCad-Logo_5mm_Copper, Symbol:KiCad-Logo_5mm_Copper, B.Cu at (201.9, 27.3)
- added TP1501: TestPoint, TestPoint:TestPoint_Keystone_5000-5004_Miniature, F.Cu at (214.1, 52.3)
- added TP1502: TestPoint, TestPoint:TestPoint_Keystone_5000-5004_Miniature, F.Cu at (202.1, 52.3)
- added TP1503: TestPoint, TestPoint:TestPoint_Keystone_5000-5004_Miniature, F.Cu at (202.1, 48.7)
- added TP1504: TestPoint, TestPoint:TestPoint_Keystone_5000-5004_Miniature, F.Cu at (186.9, 35.0)
- added TP1505: TestPoint, TestPoint:TestPoint_Keystone_5000-5004_Miniature, F.Cu at (187.2, 46.5)
- added TP1506: TestPoint, TestPoint:TestPoint_Keystone_5000-5004_Miniature, F.Cu at (171.4, 48.3)
- added TP1507: TestPoint, TestPoint:TestPoint_Keystone_5000-5004_Miniature, F.Cu at (171.4, 40.3)
- added TP1508: TestPoint, TestPoint:TestPoint_Keystone_5000-5004_Miniature, F.Cu at (171.4, 32.3)
- added TP1509: TestPoint_Small, TestPoint:TestPoint_Pad_D1.0mm, F.Cu at (211.8, 35.5)
- added TP1510: TestPoint_Small, TestPoint:TestPoint_Pad_D1.0mm, F.Cu at (205.4, 34.6)
- added TP1511: TestPoint_Small, TestPoint:TestPoint_Pad_D1.0mm, F.Cu at (191.7, 52.4)
- added TP1512: TestPoint_Small, TestPoint:TestPoint_Pad_D1.0mm, F.Cu at (189.2, 52.4)
- added TP1513: TestPoint_Small, TestPoint:TestPoint_Pad_D1.0mm, F.Cu at (194.2, 52.4)
- added TP1514: TestPoint_Small, TestPoint:TestPoint_Pad_D1.0mm, F.Cu at (196.7, 52.4)
- added U$10: MOUNTINGHOLE2.5, Adafruit 1.14-inch 240x135 Color TFT:MOUNTINGHOLE_2.5_PLATED, F.Cu at (260.9, 23.1)
- added U$4: MICROSD, Adafruit 1.14-inch 240x135 Color TFT:ADAFRUIT_3.5MM, F.Cu at (253.0, 43.5)
- added U$6: , Adafruit 1.14-inch 240x135 Color TFT:PCBFEAT-REV-040, F.Cu at (261.9, 28.0)
- added U$9: MOUNTINGHOLE2.5, Adafruit 1.14-inch 240x135 Color TFT:MOUNTINGHOLE_2.5_PLATED, F.Cu at (234.2, 23.1)
- added U1501: AP63205WU, Package_TO_SOT_SMD:TSOT-23-6, F.Cu at (187.4, 42.0)
- added U1502: TLV75733PDBV, Package_TO_SOT_SMD:SOT-23-5, F.Cu at (182.4, 34.5)
- added U2: MIC5225-3.3, Adafruit 1.14-inch 240x135 Color TFT:SOT23-5, F.Cu at (259.6, 39.4)
- added U3: 74HC4050D, Adafruit 1.14-inch 240x135 Color TFT:SOIC16, F.Cu at (253.3, 34.8)
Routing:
- net (no net): track 0.00 -> 582.7 mm, vias 0 -> 58
- net GND: track 48.7 -> 78.3 mm, vias 77 -> 108
- net /VI-: track 43.1 -> 60.6 mm, vias 77 -> 89
- net +5V: track 111.2 -> 126.3 mm, vias 8 -> 9
- net /VI+: track 0.00 -> 14.0 mm, vias 6 -> 18
- net +3V3: track 306.4 -> 312.0 mm, vias 19 -> 20
- added copper zone on F.Cu, net (none)
- added copper zone on F.Cu, net +3V3
- added copper zone on F.Cu, net +5V
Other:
- board size 123 x 75 mm -> 228.4 x 79.4 mm
- board text added: "0-80V"
- board text added: "12C"
- board text added: "12L"
- board text added: "12V"
- board text added: "3V"
- board text added: "CARPWR"
- board text added: "DC"
- board text added: "LIT"
- board text added: "MISO"
- board text added: "MOSI"
- board text added: "Mighty MPPT Power Regulation Breakout v0.1.0rc Matthew Yu & Jacob Pustilnik"
- board text added: "RST"
- board text added: "SCK"
- board text added: "SDCS"
- board text added: "ST7789 1.14""
- board text added: "TFTCS"
- board text added: "VI+"
- board text added: "VI-"
- board text added: "Vin"
- board text added: "Vin/Vlogic:3-5VDC"
- board text added: "adafruit 240x135 Color TFT"
